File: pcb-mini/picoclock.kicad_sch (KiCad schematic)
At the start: 65 parts, among them J1 UART, J10 USB, J12 LED_5V, J16 UART_S88, J2 USB_A, J3 UART, J4 xx, J5 Micro_SD_Card_Det1, J6 USB_C_Receptacle, J7 DBG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

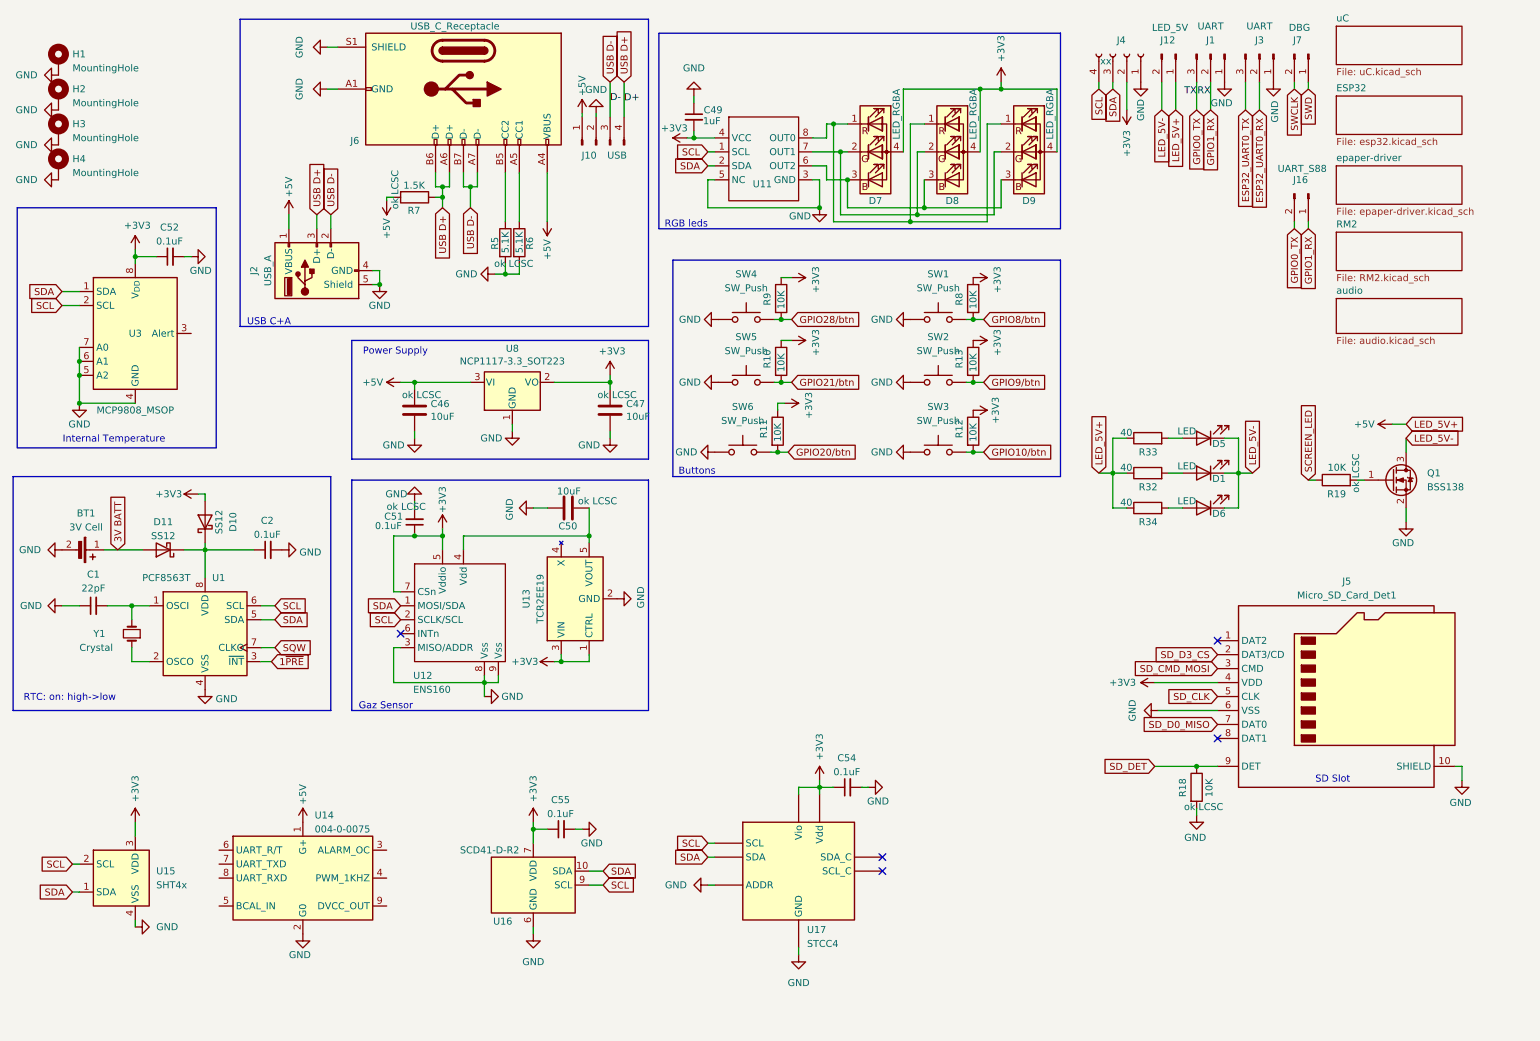
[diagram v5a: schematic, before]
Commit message: [pcb] mini: cleanup main sheet
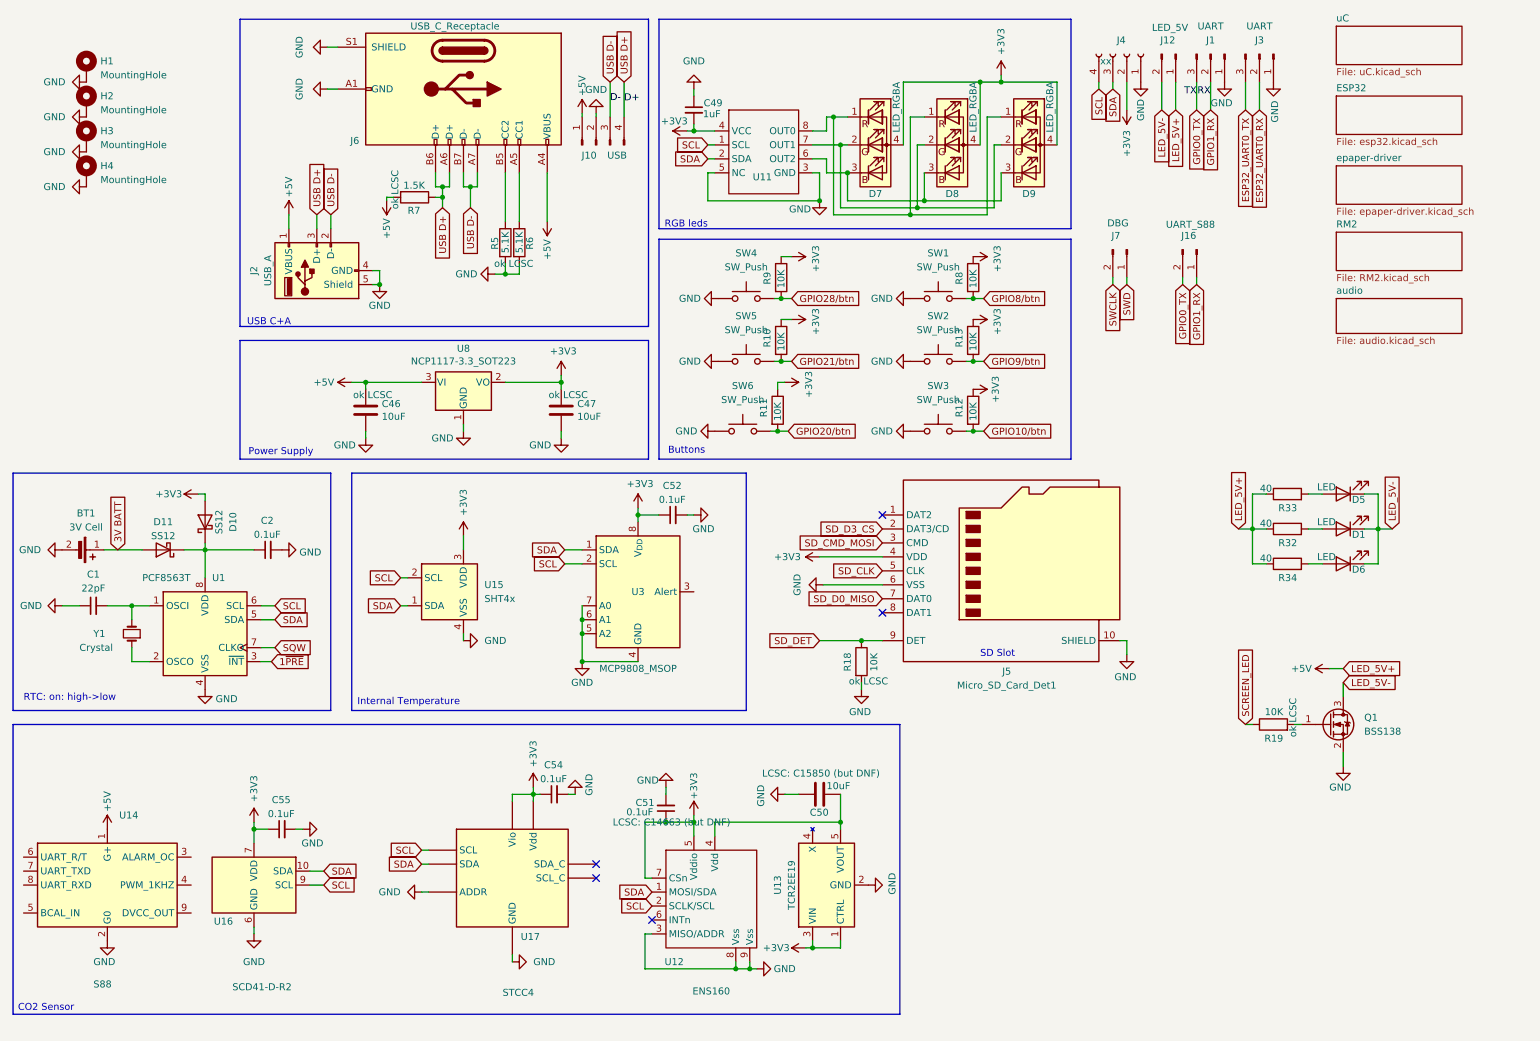
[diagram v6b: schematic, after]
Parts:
- C50: LCSC C15850 -> (none)
- C51: LCSC C14663 -> (none)
- U14: value 004-0-0075 -> S88
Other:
- note added: "CO2 Sensor"
- note removed: "Gaz Sensor"
- moved on the sheet: C46, C47, C49, C50, C51, C52, C54, C55, D1, D5, D6, D7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
